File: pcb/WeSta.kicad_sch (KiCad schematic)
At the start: 9 parts, among them J1 USB_C_Receptacle_USB2.0_16P, U1 ESP32-C3-MINI-1, U2 AW32001ECSR

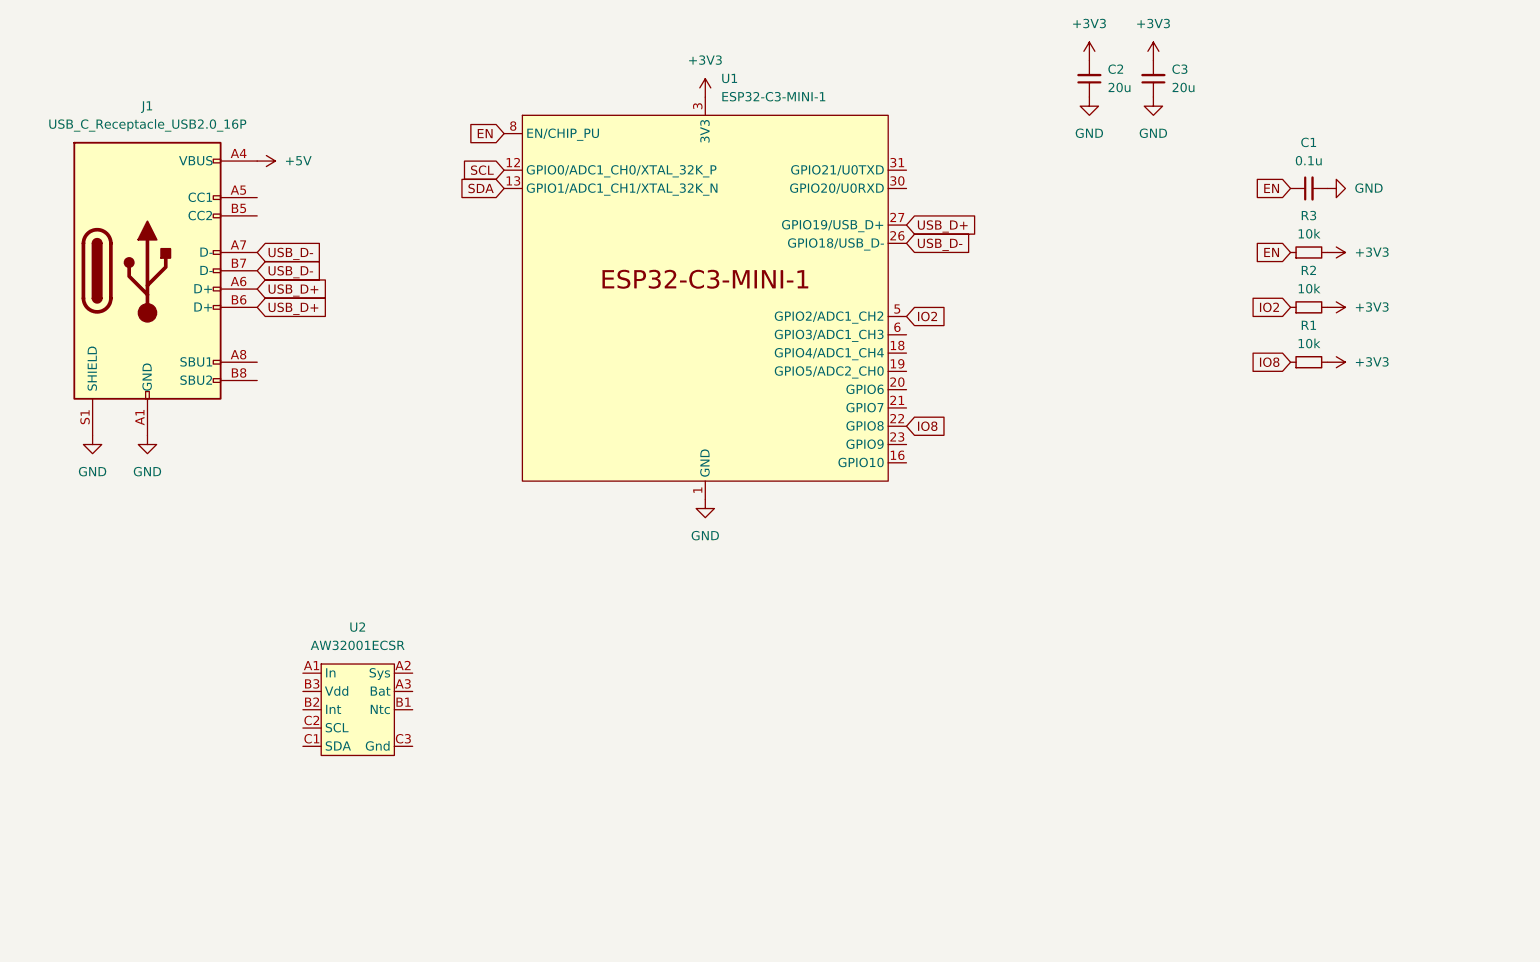
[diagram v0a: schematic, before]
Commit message: Add more sensors and start layout
- BH1730FVC
- BME280
- RG-9/11/15
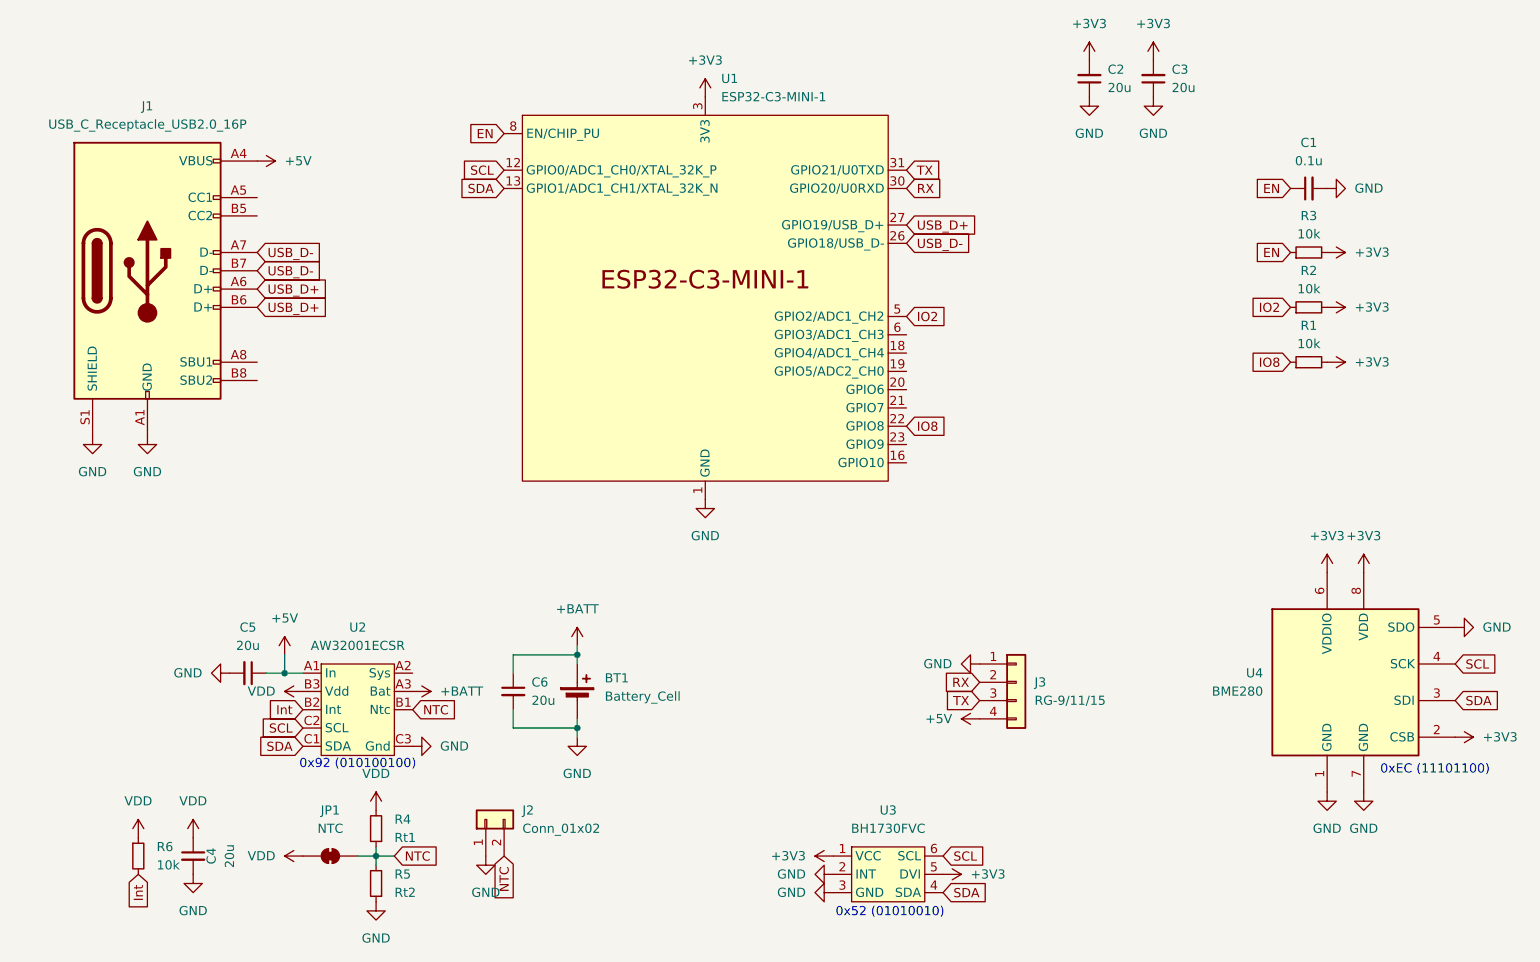
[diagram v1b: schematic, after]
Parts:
- added BT1: Battery_Cell, wirmo_power:BH-18650-B1BA002, symbol Device:Battery_Cell
- added C4, C5, C6: 20u, Capacitor_SMD:C_0603_1608Metric, symbol Device:C_Small
- added J2: Conn_01x02, Connector_PinHeader_2.54mm:PinHeader_1x02_P2.54mm_Vertical, symbol Connector_Generic:Conn_01x02
- added J3: RG-9/11/15, Connector_PinHeader_2.54mm:PinHeader_1x04_P2.54mm_Vertical, symbol Connector_Generic:Conn_01x04
- added JP1: NTC, Jumper:SolderJumper-2_P1.3mm_Bridged_RoundedPad1.0x1.5mm, symbol Jumper:SolderJumper_2_Bridged
- added R4: Rt1, Resistor_SMD:R_0603_1608Metric, symbol Device:R_Small
- added R5: Rt2, Resistor_SMD:R_0603_1608Metric, symbol Device:R_Small
- added R6: 10k, Resistor_SMD:R_0603_1608Metric, symbol Device:R_Small
- added U3: BH1730FVC, sensors:WSOF6, symbol sensors:BH1730FVC
- added U4: BME280, Package_LGA:Bosch_LGA-8_2.5x2.5mm_P0.65mm_ClockwisePinNumbering, symbol Sensor:BME280
- C1, C2, C3: footprint (none) -> Capacitor_SMD:C_0603_1608Metric
- R1, R2, R3: footprint (none) -> Resistor_SMD:R_0603_1608Metric
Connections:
- net +3V3: now also U3.1 (VCC), U3.5 (DVI), U4.2 (CSB), U4.6 (VDDIO), U4.8 (VDD)
- net +5V: now also U2.A1 (In), C5.1, J3.4 (Pin_4)
- net GND: now also U2.C3 (Gnd), BT1.2 (-), C4.2, C5.2, C6.2, J2.1 (Pin_1), J3.1 (Pin_1), R5.1, U3.2 (INT), U3.3 (GND), U4.1 (GND), U4.5 (SDO), U4.7 (GND)
- net SCL: now also U2.C2 (SCL), U3.6 (SCL), U4.4 (SCK)
- net SDA: now also U2.C1 (SDA), U3.4 (SDA), U4.3 (SDI)
- net +BATT: now reaches U2.A3 (Bat)
- net +BATT: now also BT1.1 (+), C6.1
- net NTC: now reaches U2.B1 (Ntc)
- net NTC: now also J2.2 (Pin_2), JP1.2 (B), R4.1, R5.2
- net Int: now reaches U2.B2 (Int)
- net Int: now also R6.2
- net VDD: now reaches U2.B3 (Vdd)
- net VDD: now also C4.1, JP1.1 (A), R4.2, R6.1
- net RX: now reaches U1.30 (GPIO20/U0RXD)
- net RX: now also J3.2 (Pin_2)
- net TX: now reaches U1.31 (GPIO21/U0TXD)
- net TX: now also J3.3 (Pin_3)
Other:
- note added: "0x52 (01010010)"
- note added: "0x92 (010100100)"
- note added: "0xEC (11101100)"

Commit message: Finalize rough PCB version
- Split sensors into own sub schematic as well as sub-sub sensor schematics
- Split piwer into own sub schematic
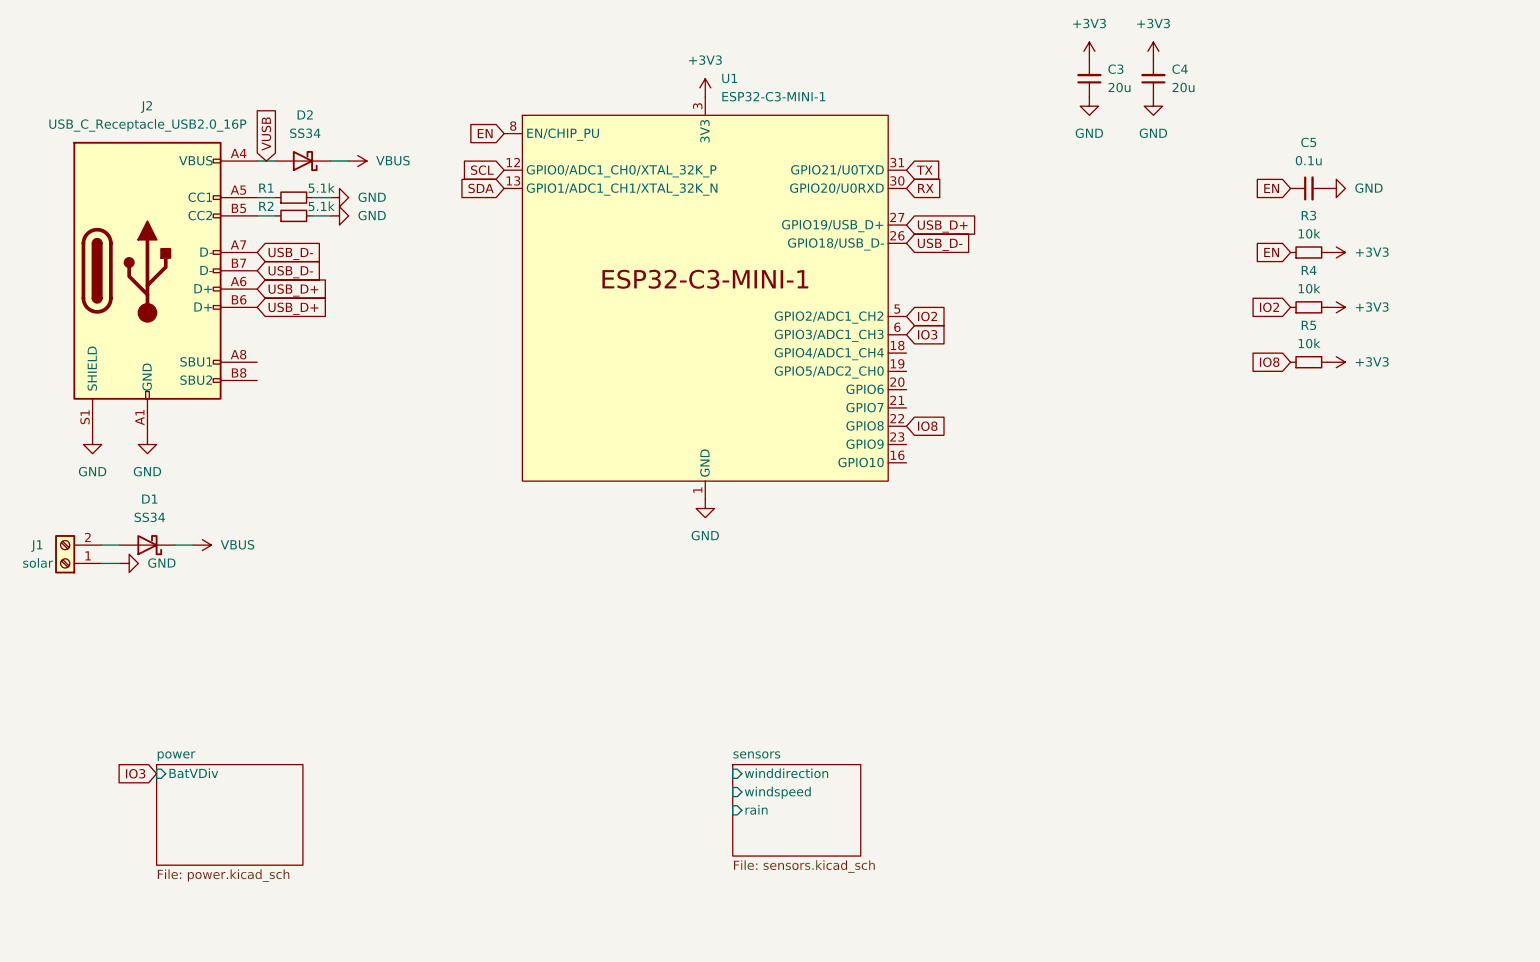
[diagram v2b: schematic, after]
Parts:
- removed BT1: Battery_Cell, wirmo_power:BH-18650-B1BA002, symbol Device:Battery_Cell
- removed C4, C5, C6: 20u, Capacitor_SMD:C_0603_1608Metric, symbol Device:C_Small
- removed J2: Conn_01x02, Connector_PinHeader_2.54mm:PinHeader_1x02_P2.54mm_Vertical, symbol Connector_Generic:Conn_01x02
- removed J3: RG-9/11/15, Connector_PinHeader_2.54mm:PinHeader_1x04_P2.54mm_Vertical, symbol Connector_Generic:Conn_01x04
- removed JP1: NTC, Jumper:SolderJumper-2_P1.3mm_Bridged_RoundedPad1.0x1.5mm, symbol Jumper:SolderJumper_2_Bridged
- removed R4: Rt1, Resistor_SMD:R_0603_1608Metric, symbol Device:R_Small
- removed R5: Rt2, Resistor_SMD:R_0603_1608Metric, symbol Device:R_Small
- removed R6: 10k, Resistor_SMD:R_0603_1608Metric, symbol Device:R_Small
- removed U2: AW32001ECSR, wirmo_power:AW32001ECSR, symbol power_wirmo:AW32001ECSR
- removed U3: BH1730FVC, sensors:WSOF6, symbol sensors:BH1730FVC
- removed U4: BME280, Package_LGA:Bosch_LGA-8_2.5x2.5mm_P0.65mm_ClockwisePinNumbering, symbol Sensor:BME280
- added D1, D2: SS34, Diode_SMD:D_SMA, symbol Diode:SS34
- added J1: solar, Connector_Phoenix_MC:PhoenixContact_MC_1,5_2-G-3.5_1x02_P3.50mm_Horizontal, symbol Connector:Screw_Terminal_01x02
- added R1, R2: 5.1k, Resistor_SMD:R_0603_1608Metric, symbol Device:R_Small
- J2: renamed from J1; footprint (none) -> Connector_USB:USB_C_Receptacle_GCT_USB4105-xx-A_16P_TopMnt_Horizontal
- renumbered C2 to C3, C3 to C4, C1 to C5, R2 to R4, R1 to R5
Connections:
- net GND: now also J1.1 (Pin_1), R1.2, R2.2
- net at J2.A5 (CC1): now also R1.1
- net at J2.B5 (CC2): now also R2.1
- net IO3: now reaches U1.6 (GPIO3/ADC1_CH3)
- net +5V renamed VUSB
- net VUSB: now also D2.2 (A)
- new net: D1.2 (A), J1.2 (Pin_2)
- new net VBUS: D1.1 (K), D2.1 (K)
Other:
- added sheet power (power.kicad_sch)
- added sheet sensors (sensors.kicad_sch)
- note removed: "0x52 (01010010)"
- note removed: "0x92 (010100100)"
- note removed: "0xEC (11101100)"
